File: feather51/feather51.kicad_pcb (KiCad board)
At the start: 2 copper layers, 22.9 x 50.8 mm, 34 parts, among them J1 BATTERY, J2 USB_B_Micro, J3 Conn_01x12, J4 C2D, J5 Conn_01x16, SW1 RESET, U1 SPX3819M5-L-3-3, U2 EFM8UB10F16G-C-QFN28, U3 MCP73831-2-OT

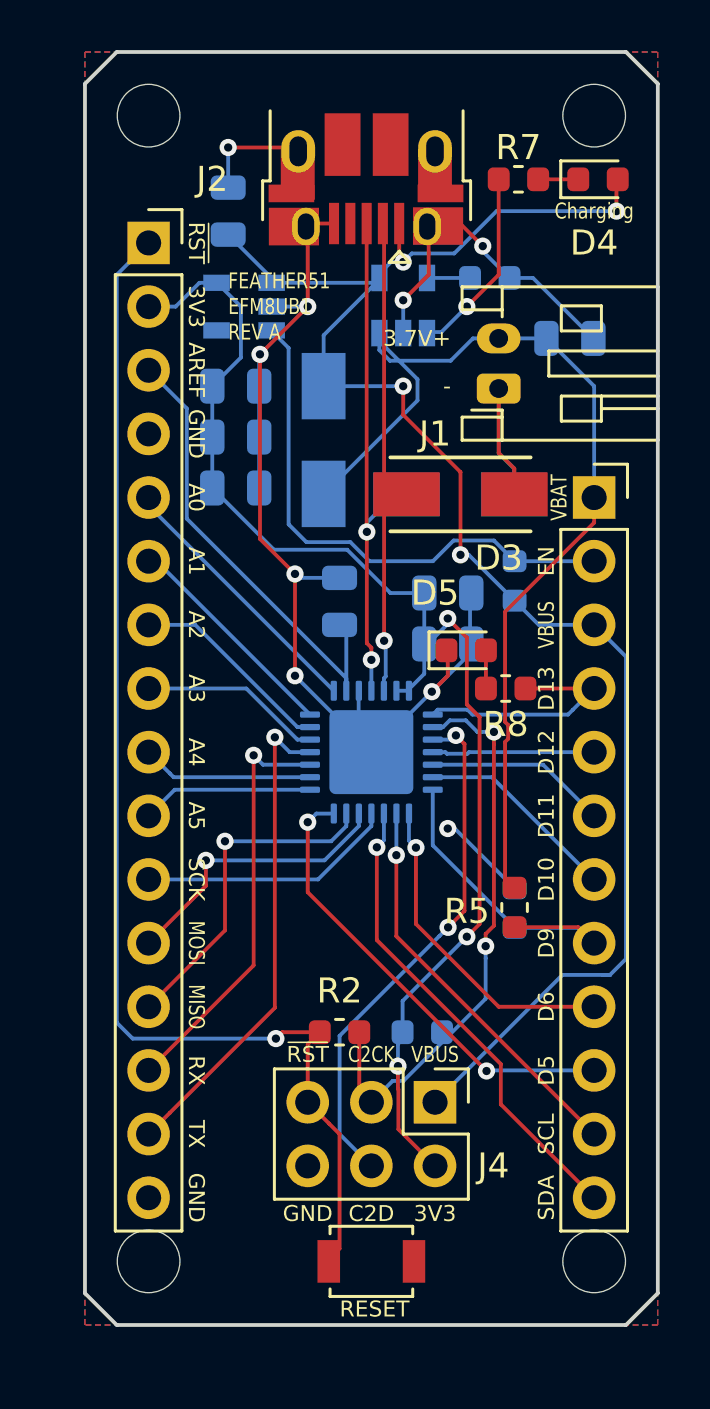
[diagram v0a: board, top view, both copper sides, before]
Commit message: 0.7mil spacing is wrong
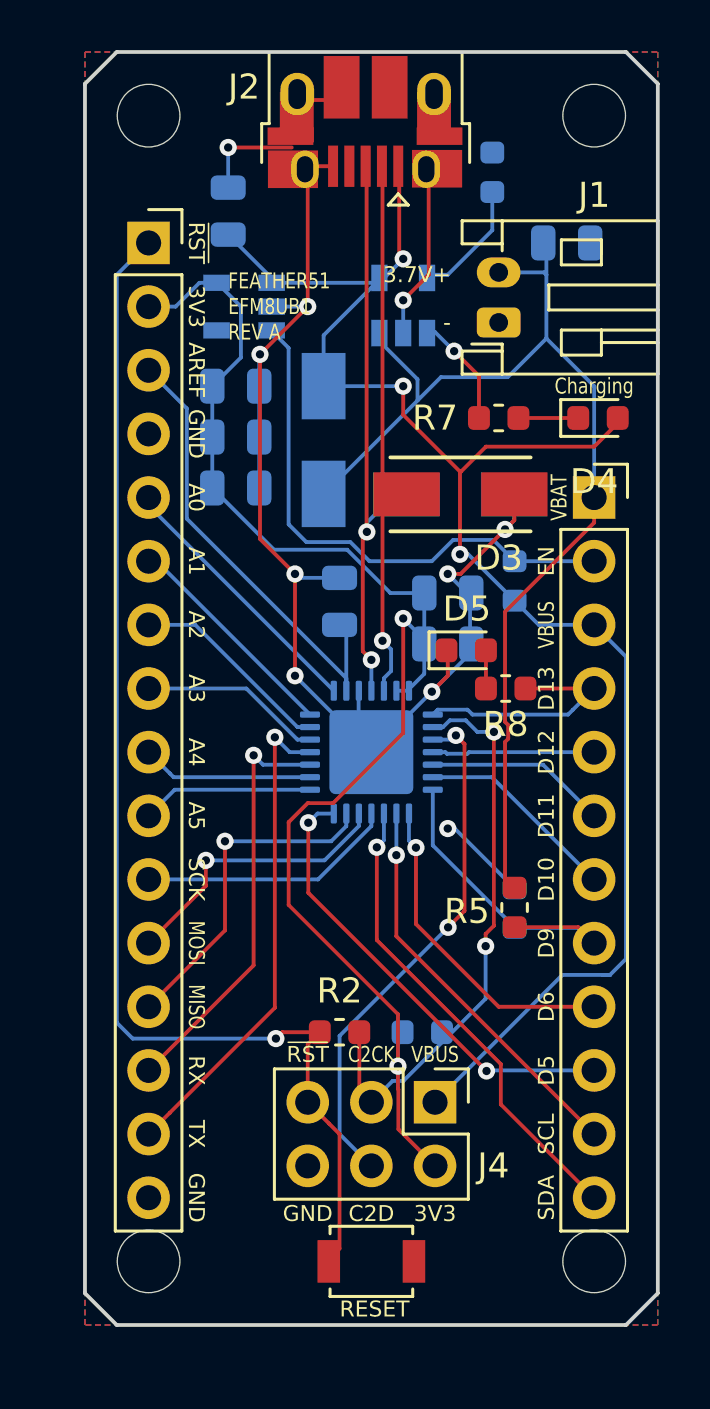
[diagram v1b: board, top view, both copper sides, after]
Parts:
- moved R7 9.56 mm to (141.0, 57.8)
- moved D4 9.52 mm to (144.9, 57.8)
- moved R4 4.22 mm to (140.7, 48.0), turned to 90 degrees
- moved C8 3.81 mm to (143.7, 50.8)
- moved J1 2.63 mm to (141.0, 54.0)
- moved J2 2.29 mm to (135.6, 46.0)
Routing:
- net /VBAT: track 40.8 -> 45.1 mm
- net GND: track 75.2 -> 71.1 mm, vias 9 -> 10
- net +3V3: track 52.1 -> 56.2 mm, vias 3 -> 2
- net Net-(R7-Pad2): track 7.42 -> 4.41 mm
- net Net-(R4-Pad1): track 1.84 -> 4.80 mm
- net VBUS: track 68.0 -> 65.8 mm, vias 4 -> 3
- net /D+: track 21.2 -> 23.1 mm
- net /D-: track 19.7 -> 21.6 mm
- net Net-(D4-Pad1): track 1.60 -> 2.54 mm

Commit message: Layout locked
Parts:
- moved J5 2.54 mm to (124.5, 50.8)
- moved REF** 1.80 mm to (143.5, 47.0)
- moved J4 1.80 mm to (137.2, 86.4)
- moved REF** 1.80 mm to (143.5, 92.7)
- moved REF** 1.80 mm to (125.7, 47.0)
- moved REF** 1.80 mm to (125.7, 92.7)
- moved SW1 1.80 mm to (134.6, 92.7)
- moved J2 1.48 mm to (134.9, 47.2)
- moved R2 1.02 mm to (134.6, 81.3)
- moved C1 0.38 mm to (129.8, 49.5)
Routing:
- net /~RESET: track 50.2 -> 59.7 mm, vias 1 -> 0
- net +3V3: track 56.2 -> 60.2 mm
- net /C2CK: track 23.1 -> 27.1 mm
- net VBUS: track 65.8 -> 68.6 mm, vias 3 -> 5
- net /SCK: track 10.3 -> 12.8 mm
- net /MOSI: track 11.4 -> 14.0 mm
- net /MISO: track 13.5 -> 16.0 mm
- net /D1: track 19.6 -> 22.1 mm
- net /D0: track 16.7 -> 19.3 mm
- net /AREF: track 18.8 -> 21.3 mm
- net /A5: track 6.87 -> 9.41 mm
- net /A4: track 6.85 -> 9.39 mm
- net /A3: track 7.28 -> 9.82 mm
- net /A2: track 8.13 -> 10.7 mm
- net /A1: track 8.97 -> 11.5 mm
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
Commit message: Released to Manufacturing
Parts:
- D1: value 1N5817 -> D1
- D2: value 1N5817 -> D2
- D3: value 1N5817 -> D3
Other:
- board text added: "jeremy@synack.me"

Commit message: Update diode and LDO part numbers to match as-built revision A boards
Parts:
- removed REF** (x4): MountingHole_2.5mm, MountingHole:MountingHole_2.5mm
- D1: value D1 -> SS12
- D2: value D2 -> SS12
- D3: value D3 -> SS12
- U1: value SPX3819M5-L-3-3 -> LP2985-33DBVR
